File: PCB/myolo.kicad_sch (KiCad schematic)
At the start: 54 parts, among them J1 SiPM1 Connector, J2 SiPM2 Connector, J3 Conn_01x03_Socket, J4 Conn_01x03_Socket, U1 LM6172, U2 LM6172, U3 YAAJ_BluePill

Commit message: updated schematics settings
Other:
- title: Myolo Amp+Peak Hold -> Myolo PCBs
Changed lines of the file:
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@@
 	(paper "A4")
 	(title_block
-		(title "Myolo Amp+Peak Hold")
-		(date "2025-08-08")
+		(title "Myolo PCBs")
+		(date "2025-12-30")
 		(rev "1")
 		(company "Nico Entz")

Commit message: Widerstandswerte angepasst
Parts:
- R14, R15: value 50 -> 47
- R4, R9: value 20k -> 22k
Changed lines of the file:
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@@
 			)
 		)
-		(property "Value" "20k"
+		(property "Value" "22k"
 			(at 232.41 74.9299 0)
 			(effects
@@
 			)
 		)
-		(property "Value" "20k"
+		(property "Value" "22k"
 			(at 232.41 142.2399 0)
 			(effects
@@
 			)
 		)
-		(property "Value" "50"
+		(property "Value" "47"
 			(at 21.336 48.768 0)
 			(effects
@@
 			)
 		)
-		(property "Value" "50"
+		(property "Value" "47"
 			(at 54.356 48.768 0)
 			(effects

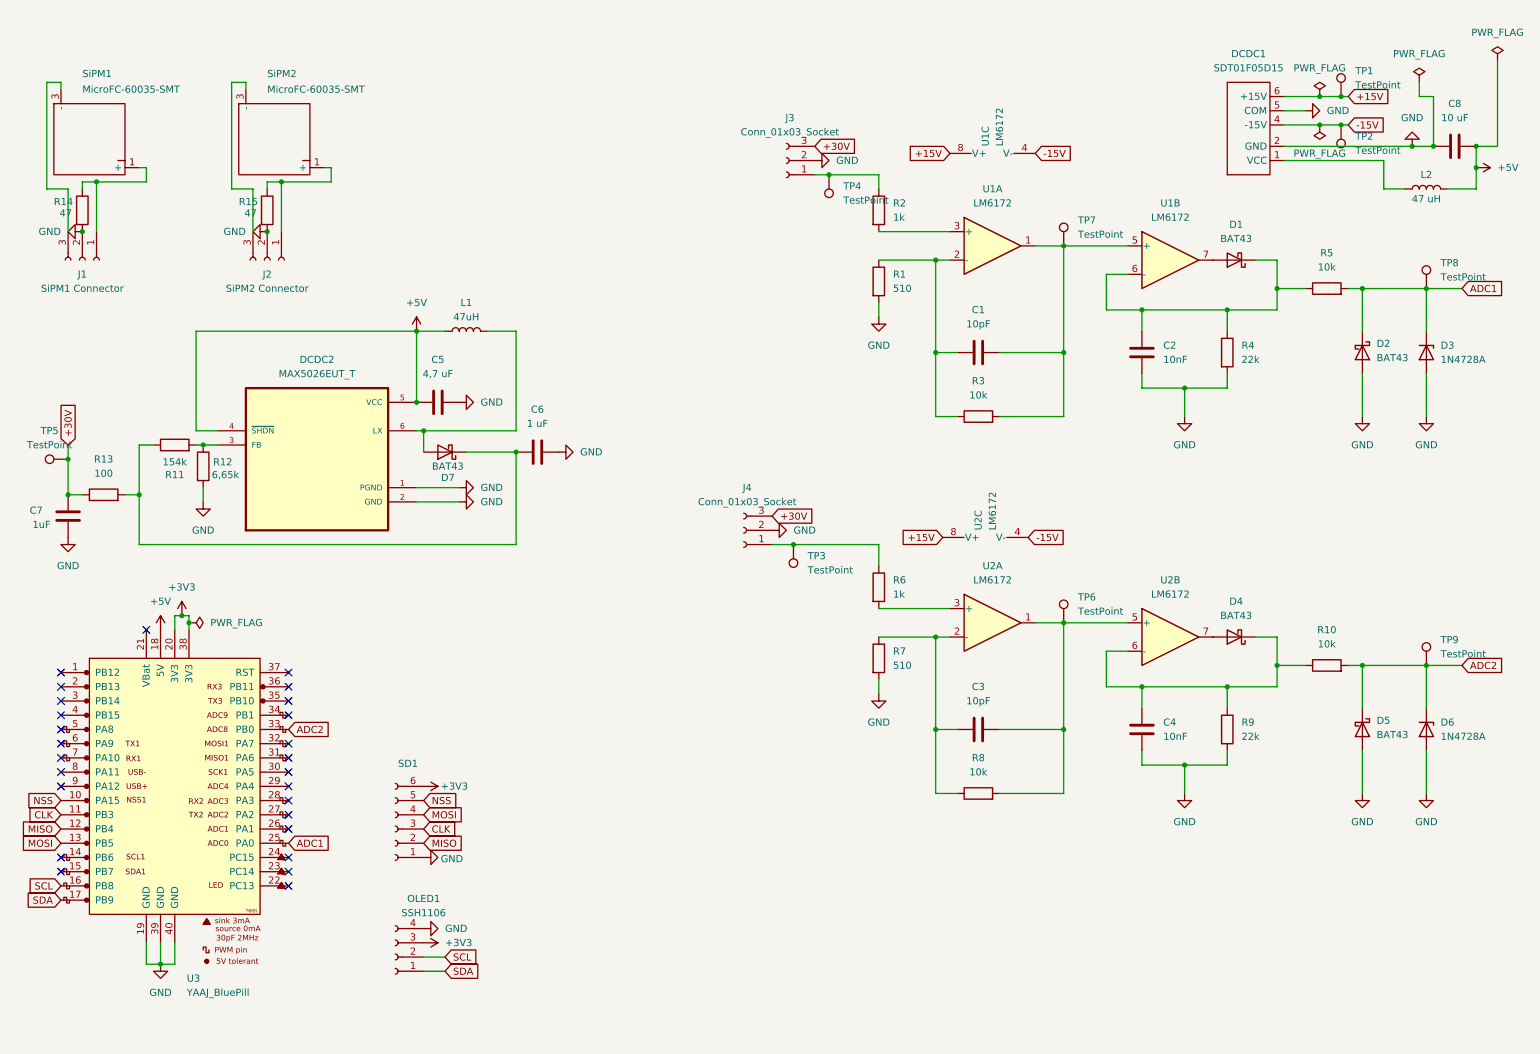
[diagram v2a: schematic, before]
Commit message: added bom
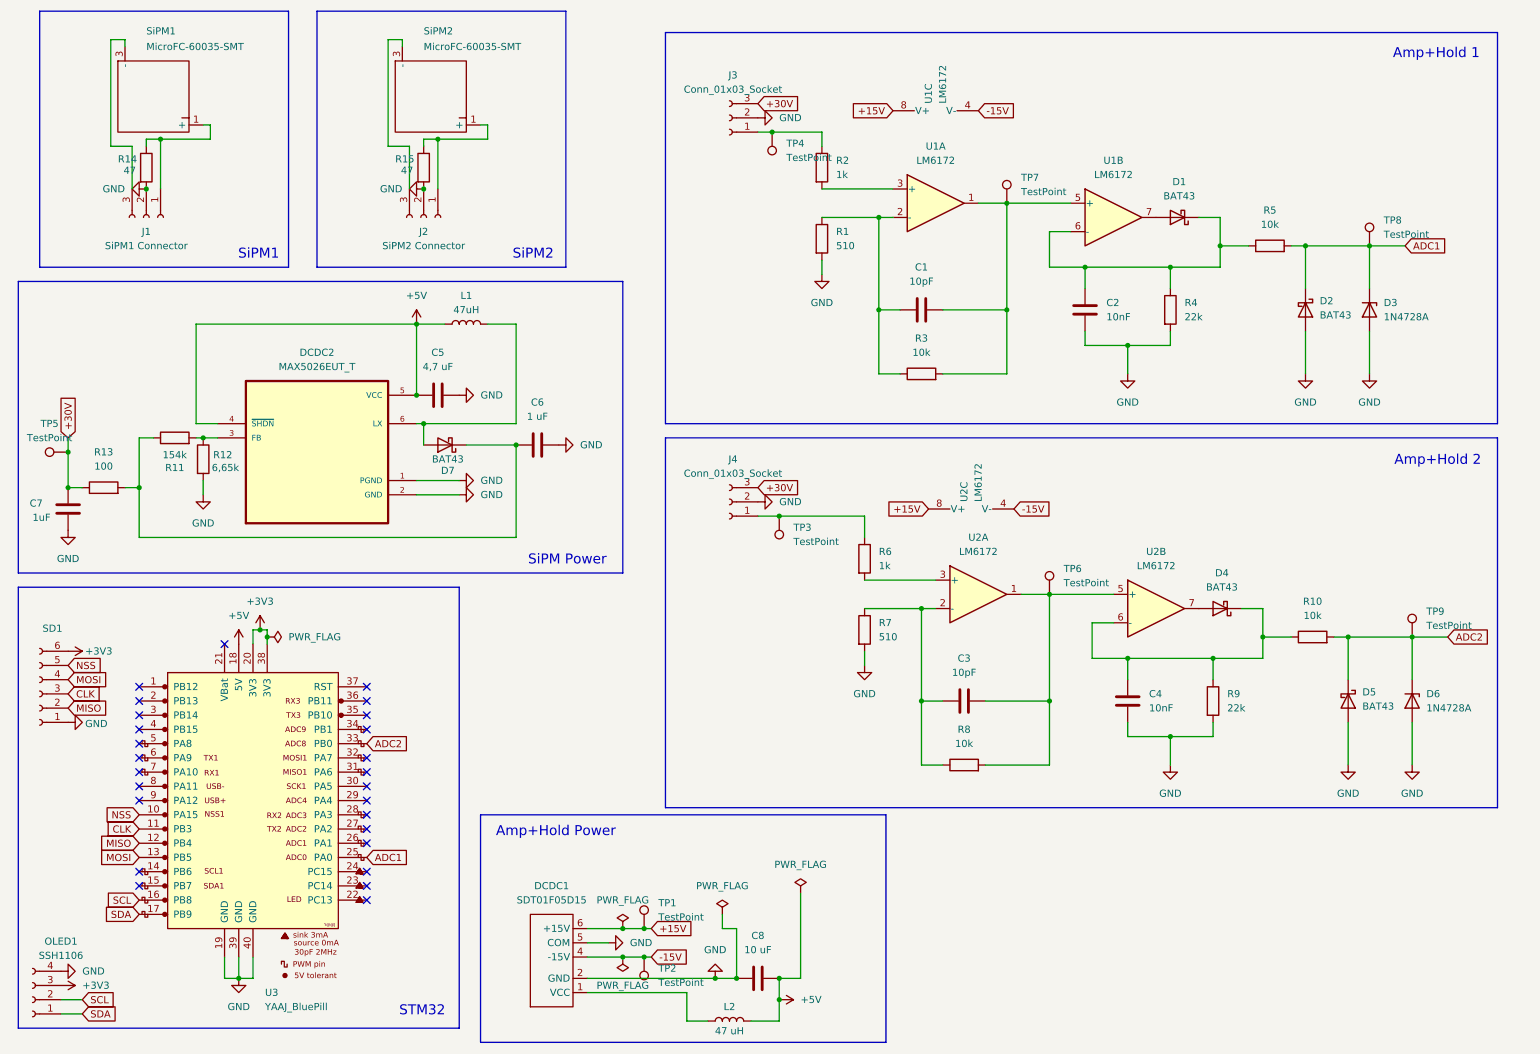
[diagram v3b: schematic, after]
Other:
- note added: "Amp+Hold 1"
- note added: "Amp+Hold 2"
- note added: "Amp+Hold Power"
- note added: "STM32"
- note added: "SiPM Power"
- note added: "SiPM1"
- note added: "SiPM2"
- moved on the sheet: C1, C2, C3, C4, C5, C6, C7, C8, D1, D2, D3, D4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

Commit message: added GND test point to pcb
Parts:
- added TP0: TestPoint, TestPoint:TestPoint_Pad_1.0x1.0mm, symbol Connector:TestPoint
- SiPM1, SiPM2: footprint Custom:SiPM -> Custom:SiPM3
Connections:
- net GND: now also TP0.1
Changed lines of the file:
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@@
 	)
 	(junction
+		(at 50.8 184.15)
+		(diameter 0)
+		(color 0 0 0 0)
+	)
+	(junction
 		(at 46.99 88.9)
 		(diameter 0)
@@
 	(wire
 		(pts
-			(xy 50.8 181.61) (xy 50.8 185.42)
+			(xy 50.8 181.61) (xy 50.8 184.15)
 		)
 		(stroke
@@
 	(wire
 		(pts
+			(xy 50.8 184.15) (xy 50.8 185.42)
+		)
+		(stroke
+			(width 0)
+			(type default)
+		)
+	)
+	(wire
+		(pts
 			(xy 262.89 124.46) (xy 269.24 124.46)
 		)
@@
 	(wire
 		(pts
+			(xy 48.26 184.15) (xy 50.8 184.15)
+		)
+		(stroke
+			(width 0)
+			(type default)
+		)
+	)
+	(wire
+		(pts
 			(xy 175.26 135.89) (xy 175.26 147.32)
 		)
@@
 			)
 		)
-		(property "Footprint" "Custom:SiPM"
+		(property "Footprint" "Custom:SiPM3"
 			(at 31.75 34.29 0)
 			(effects
@@
 	)
 	(symbol
+		(lib_id "Connector:TestPoint")
+		(at 48.26 184.15 90)
+		(unit 1)
+		(exclude_from_sim no)
+		(in_bom yes)
+		(on_board yes)
+		(dnp no)
+		(fields_autoplaced yes)
+		(property "Reference" "TP0"
+			(at 44.958 179.07 90)
+			(effects
+				(font
+					(size 1.27 1.27)
+				)
+			)
+		)
+		(property "Value" "TestPoint"
+			(at 44.958 181.61 90)
+			(effects
+				(font
+					(size 1.27 1.27)
+				)
+			)
+		)
+		(property "Footprint" "TestPoint:TestPoint_Pad_1.0x1.0mm"
+			(at 48.26 179.07 0)
+			(effects
+				(font
+					(size 1.27 1.27)
+				)
+				(hide yes)
+			)
+		)
+		(property "Datasheet" "~"
+			(at 48.26 179.07 0)
+			(effects
+				(font
+					(size 1.27 1.27)
+				)
+				(hide yes)
+			)
+		)
+		(property "Description" "test point"
+			(at 48.26 184.15 0)
+			(effects
+				(font
+					(size 1.27 1.27)
+				)
+				(hide yes)
+			)
+		)
+		(pin "1"
+		)
+		(instances
+			(project "myolo"
+				(path "/dc0990d6-dfea-4502-9a83-5fe7d15ba70a"
+					(reference "TP0")
+					(unit 1)
+				)
+			)
+		)
+	)
+	(symbol
 		(lib_id "Device:R")
 		(at 245.11 124.46 90)
@@
 			)
 		)
-		(property "Footprint" "Custom:SiPM"
+		(property "Footprint" "Custom:SiPM3"
 			(at 81.28 34.29 0)
 			(effects

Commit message: updated pcb
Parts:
- SD1: footprint Custom:1x6 NoGND -> Custom:SdHEAD
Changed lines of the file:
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@@
 			)
 		)
-		(property "Footprint" "Custom:1x6 NoGND"
+		(property "Footprint" "Custom:SdHEAD"
 			(at 17.78 134.62 0)
 			(effects
